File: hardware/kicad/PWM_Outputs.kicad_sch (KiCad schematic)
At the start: 3 parts

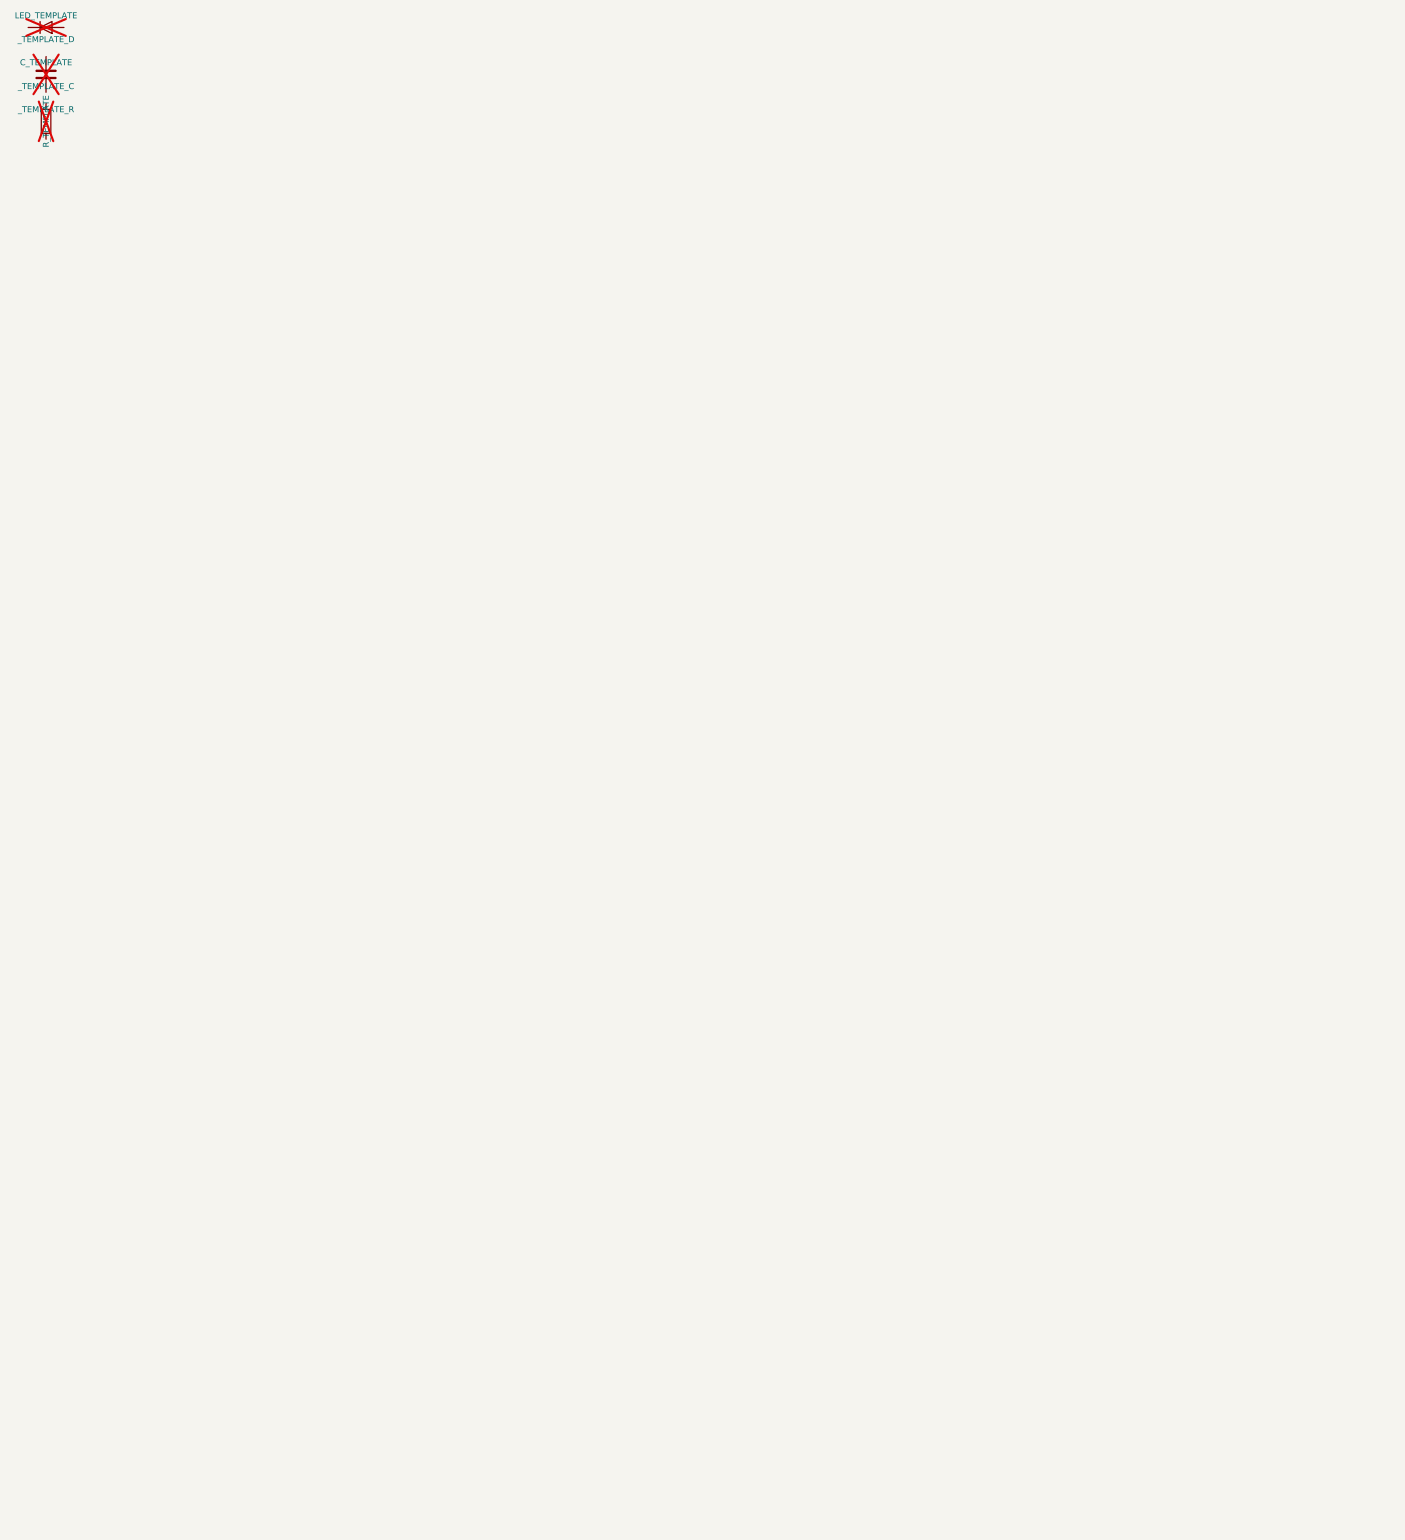
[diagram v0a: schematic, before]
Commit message: Phase A3: hierarchical V1 schematic generated from pstxnet.dat, ERC clean, netlist == pstxnet
gen_symbols.py (R1240N001x, TCAN1042H-Q1, CMS06 diode, VIN_RAW power symbol per current datasheets),
kicad_sym.py (flattened embedding of KiCad 9 library symbols), gen_sch.py (7 sub-sheets mirroring the OrCAD
blocks, labels/hierarchical pins/power symbols, deterministic symbol paths shared with the PCB via v1_design.py),
check_netlist.py (schematic and board nets == pstxnet.dat, refs and footprint paths match).
ERC 0 violations with --severity-all. Allegro refdes without a trailing digit get a '1' suffix (KiCad annotation
rule); original kept in the Allegro_RefDes property.

Co-Authored-By: Claude Fable 5.1 <noreply@anthropic.com>
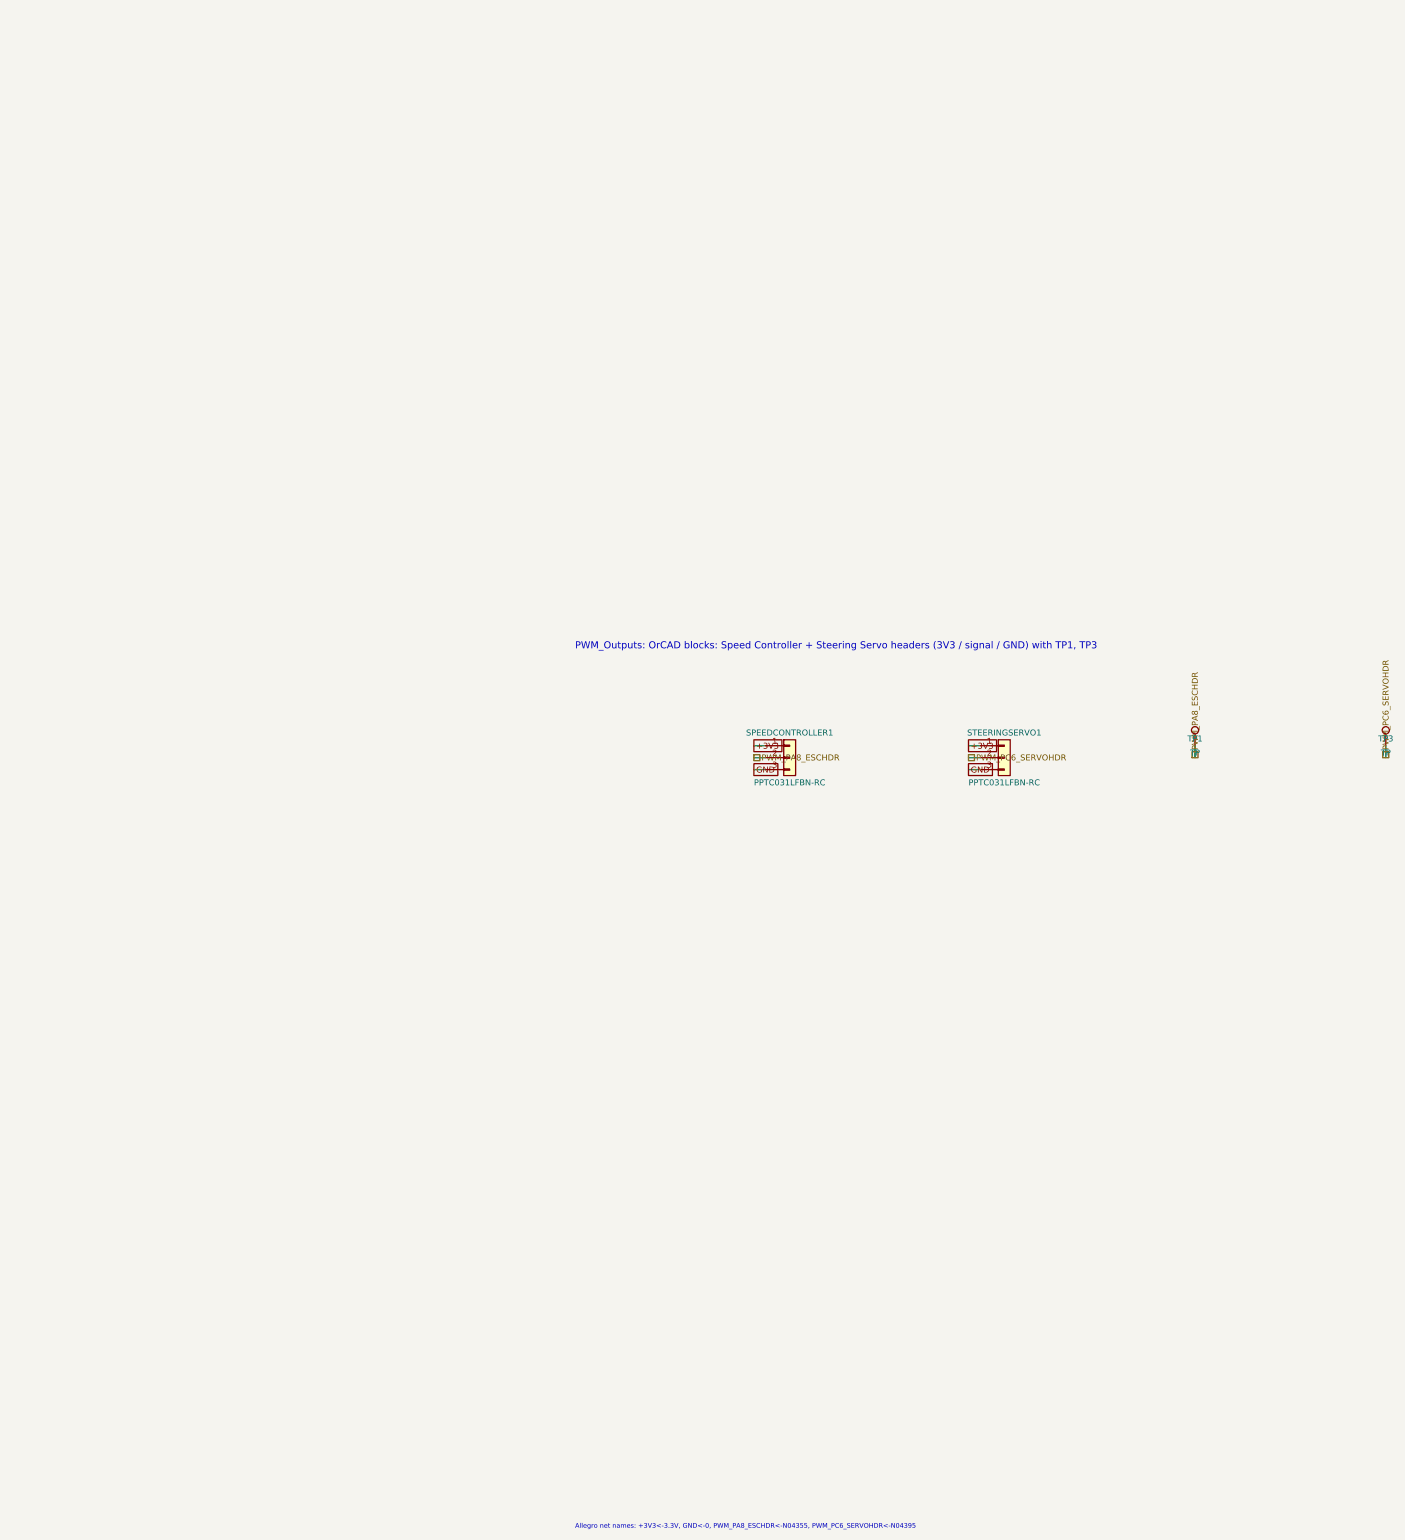
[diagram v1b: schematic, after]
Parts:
- removed _TEMPLATE_C: C_TEMPLATE, symbol Device:C
- removed _TEMPLATE_D: LED_TEMPLATE, symbol Device:LED
- removed _TEMPLATE_R: R_TEMPLATE, symbol Device:R
- added SPEEDCONTROLLER1, STEERINGSERVO1: PPTC031LFBN-RC, LoRa_Boat_Controller:CONN_PPTC031_SUL, symbol Connector_Generic:Conn_01x03
- added TP1, TP3: TP, LoRa_Boat_Controller:amv_test_point, symbol Connector:TestPoint
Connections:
- new net +3V3: SPEEDCONTROLLER1.1 (Pin_1), STEERINGSERVO1.1 (Pin_1)
- new net GND: SPEEDCONTROLLER1.3 (Pin_3), STEERINGSERVO1.3 (Pin_3)
- new net PWM_PA8_ESCHDR: SPEEDCONTROLLER1.2 (Pin_2), TP1.1
- new net PWM_PC6_SERVOHDR: STEERINGSERVO1.2 (Pin_2), TP3.1
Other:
- note added: "Allegro net names: +3V3<-3.3V, GND<-0, PWM_PA8_ESCHDR<-N04355, PWM_PC6_SERVOHDR<-N04395"
- note added: "PWM_Outputs: OrCAD blocks: Speed Controller + Steering Servo headers (3V3 / signal / GND) with TP1, TP3"
- company: (none) -> University of Arkansas EECS
- title: (none) -> LoRa Autonomous Boat Controller V1 - PWM_Outputs

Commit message: Phase A3 close: CANH/CANL net names corrected, BOM with MPNs, DSN-v2 comparison, schematic exports
- gen_pcb.py: N04855 is CANL (U5 pin 6) and N24691 is CANH (U5 pin 7) per pstxnet.dat + TI SLLSES9D; the
  old NETLIST.md had them reversed (Codex review finding R03).
- gen_bom.py: docs/BOM.csv regenerated from the schematic with MPN/manufacturer/description/confidence/price
  columns (research in docs/research/BOM_MPN_RESEARCH.md, prices 2026-09-16).
- a0_xor_dsn.py: DSN v2 copper vs v5 films = 54 % / 63 % mismatch, 0 of 20 vias coincide, 0 of 45 parts unmoved;
  the DSN wiring is unusable for v5 (documented in docs/A0_PROVENANCE.md).
- Schematic PDF and per-sheet SVG exports in docs/img.
Gates: DRC 0 errors / 0 unconnected, ERC 0 violations, netlist check PASS, XOR F.Cu 0.87 % B.Cu 0.23 %.

Co-Authored-By: Claude Fable 5.1 <noreply@anthropic.com>
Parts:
- SPEEDCONTROLLER1, STEERINGSERVO1: MPN (none) -> PPTC031LFBN-RC; Manufacturer (none) -> Sullins Connector Solutions
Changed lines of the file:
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@@
 			)
 		)
-		(property "Description" "Generic connector, single row, 01x03, script generated (kicad-library-utils/schlib/autogen/connector/)"
+		(property "Description" "1x3 2.54 mm female header, through-hole"
 			(at 58.42 35.56 0)
 			(effects
@@
 		)
 		(property "Allegro_Device" "PPTC031LFBN-RC_CONN_PPTC031_SUL_CONN_PPTC031"
+			(at 58.42 35.56 0)
+			(effects
+				(font
+					(size 1.27 1.27)
+				)
+				(hide yes)
+			)
+		)
+		(property "MPN" "PPTC031LFBN-RC"
+			(at 58.42 35.56 0)
+			(effects
+				(font
+					(size 1.27 1.27)
+				)
+				(hide yes)
+			)
+		)
+		(property "Manufacturer" "Sullins Connector Solutions"
 			(at 58.42 35.56 0)
 			(effects
@@
 			)
 		)
-		(property "Description" "Generic connector, single row, 01x03, script generated (kicad-library-utils/schlib/autogen/connector/)"
+		(property "Description" "1x3 2.54 mm female header, through-hole"
 			(at 104.14 35.56 0)
 			(effects
@@
 		)
 		(property "Allegro_Device" "PPTC031LFBN-RC_CONN_PPTC031_SUL_CONN_PPTC031"
+			(at 104.14 35.56 0)
+			(effects
+				(font
+					(size 1.27 1.27)
+				)
+				(hide yes)
+			)
+		)
+		(property "MPN" "PPTC031LFBN-RC"
+			(at 104.14 35.56 0)
+			(effects
+				(font
+					(size 1.27 1.27)
+				)
+				(hide yes)
+			)
+		)
+		(property "Manufacturer" "Sullins Connector Solutions"
 			(at 104.14 35.56 0)
 			(effects
@@
 			)
 		)
-		(property "Description" "test point"
+		(property "Description" "Bare plated test-point pad 3.4 mm / 1.4 mm hole (no part; Keystone 5020 would need a footprint change)"
 			(at 144.78 33.02 0)
 			(effects
@@
 		)
 		(property "Allegro_Device" "TEST POINT_AMV_TEST_POINT_TEST POINT"
+			(at 144.78 33.02 0)
+			(effects
+				(font
+					(size 1.27 1.27)
+				)
+				(hide yes)
+			)
+		)
+		(property "MPN" ""
+			(at 144.78 33.02 0)
+			(effects
+				(font
+					(size 1.27 1.27)
+				)
+				(hide yes)
+			)
+		)
+		(property "Manufacturer" ""
 			(at 144.78 33.02 0)
 			(effects
@@
 			)
 		)
-		(property "Description" "test point"
+		(property "Description" "Bare plated test-point pad 3.4 mm / 1.4 mm hole (no part; Keystone 5020 would need a footprint change)"
 			(at 185.42 33.02 0)
 			(effects
@@
 			(at 185.42 33.02 0)
 			(effects
+				(font
+					(size 1.27 1.27)
+				)
+				(hide yes)
+			)
+		)
+		(property "MPN" ""
+			(at 185.42 33.02 0)
+			(effects
+				(font
+					(size 1.27 1.27)
+				)
+				(hide yes)
+			)
+		)
+		(property "Manufacturer" ""
+			(at 185.42 33.02 0)
+			(effects
